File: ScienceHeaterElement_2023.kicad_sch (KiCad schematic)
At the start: 9 parts, among them Q1 NPN, U1 LMT85DCK

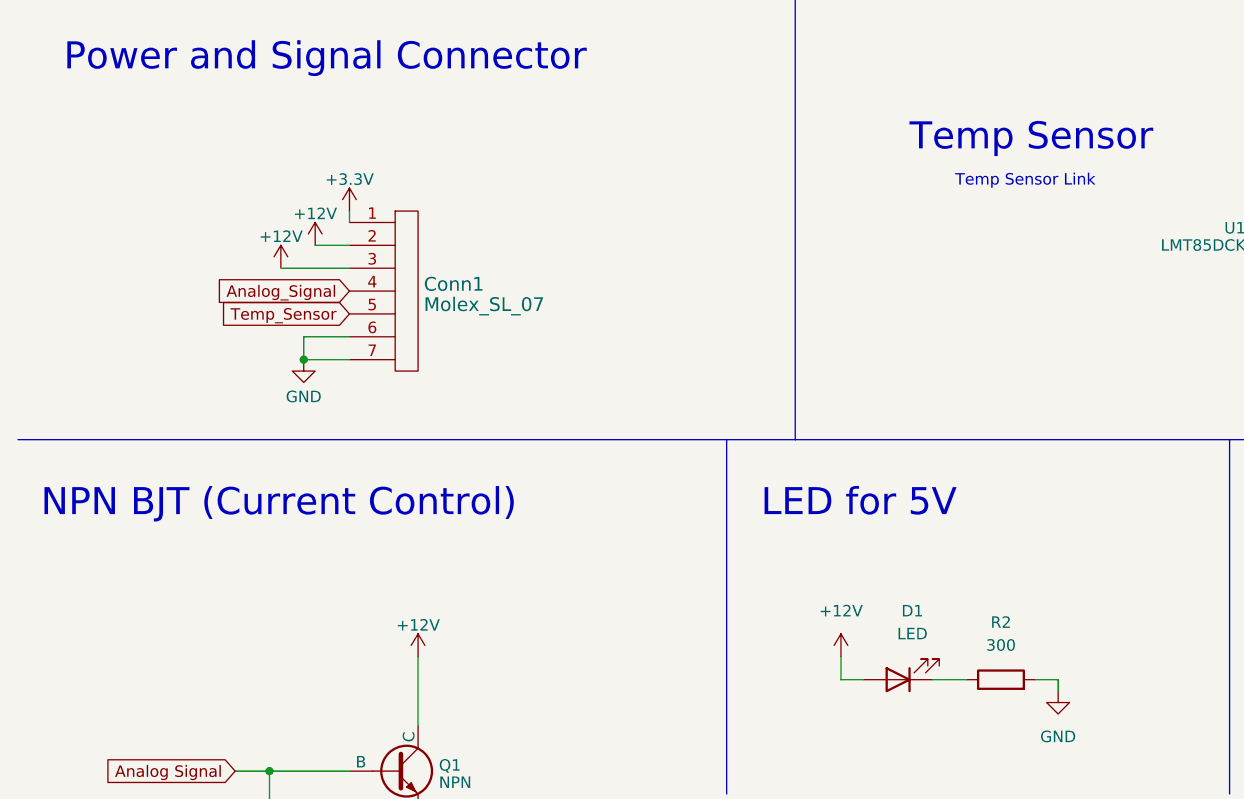
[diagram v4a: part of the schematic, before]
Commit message: Changed LED power and Molex 7 pin
Changed LED power from two 12V to a 12V and a 3.3V to indicate power of the two lines, and changed the molex 7 pin connector to a 3 pin and a 4 pin
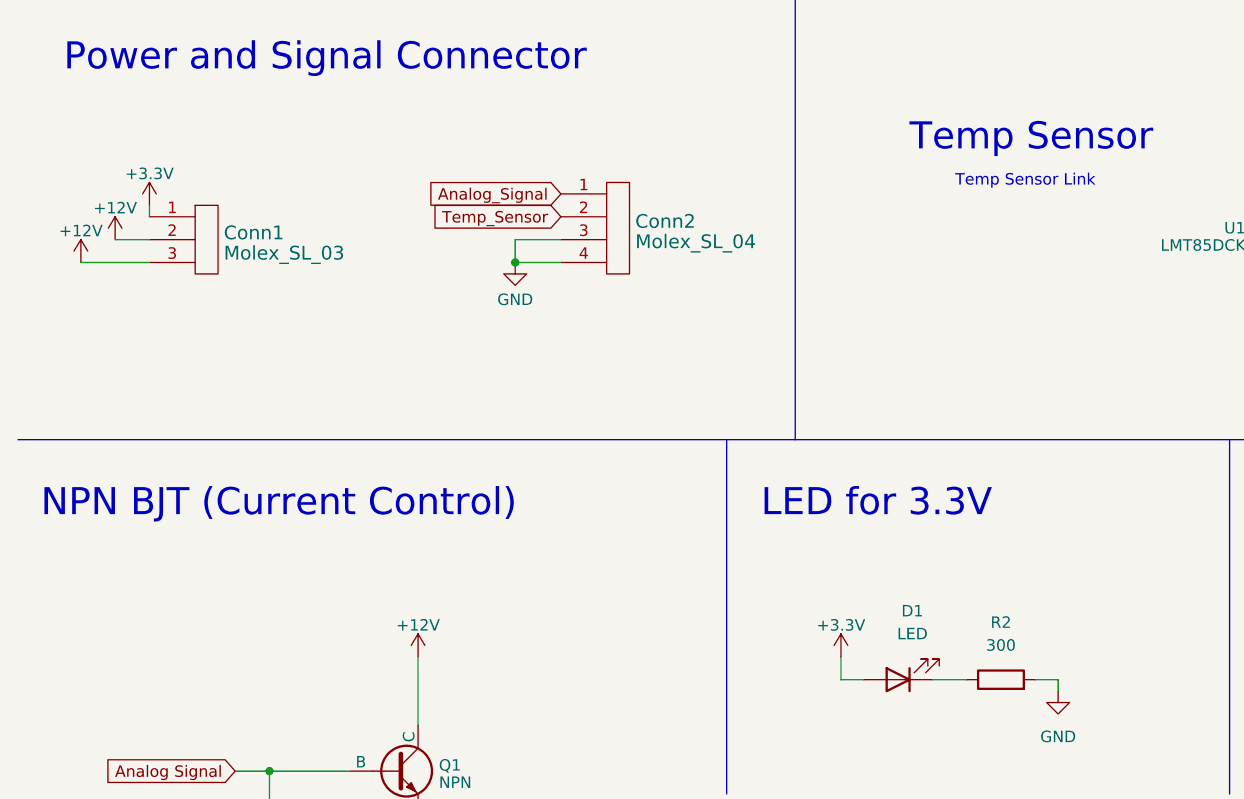
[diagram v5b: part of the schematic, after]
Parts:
- removed Conn1: Molex_SL_07, symbol MRDT_Connectors:Molex_SL_07
- added Conn1: Molex_SL_03, symbol MRDT_Connectors:Molex_SL_03
- added Conn2: Molex_SL_04, symbol MRDT_Connectors:Molex_SL_04
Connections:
- net +12V: now also Conn1.2, Conn1.3; no longer D1.2 (A)
- net +3.3V: now also D1.2 (A), Conn1.1
- net Analog_Signal: now also Conn2.1
- net GND: now also Conn2.3, Conn2.4
- net Temp_Sensor: now also Conn2.2
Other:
- note removed: "LED for 5V"

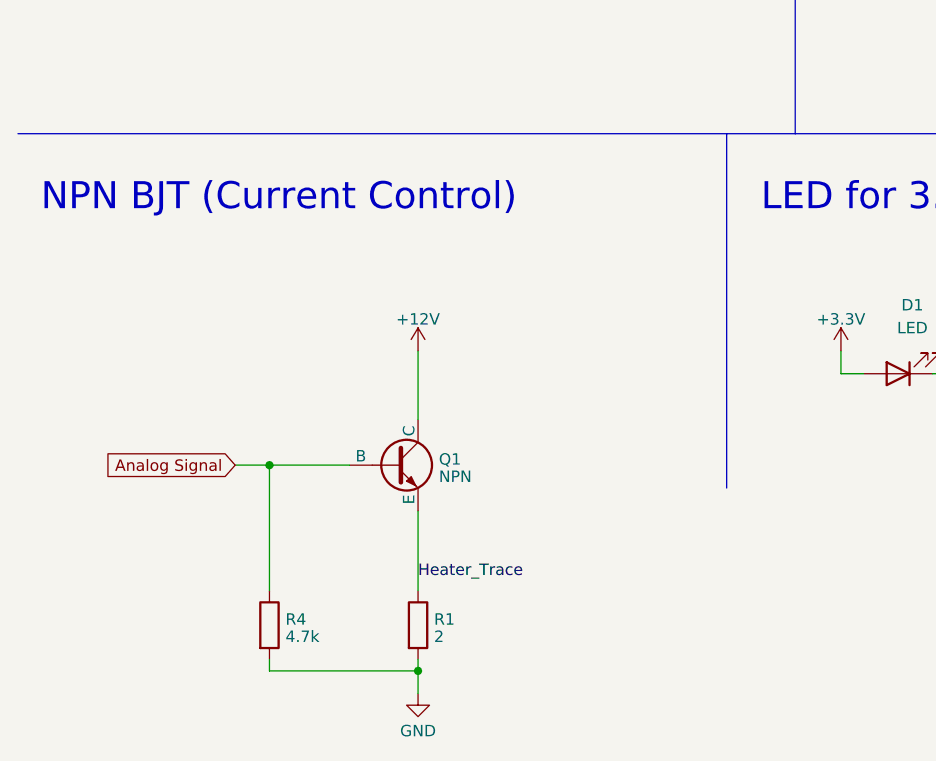
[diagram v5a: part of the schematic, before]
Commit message: Switched BJT to MOSFET
Switched to a MOSFET from a BJT. The testing for the BJT gave us unusable results for controlling the current flow through the BJT so we switched to a MOSFET which allows easier controls of the heating element
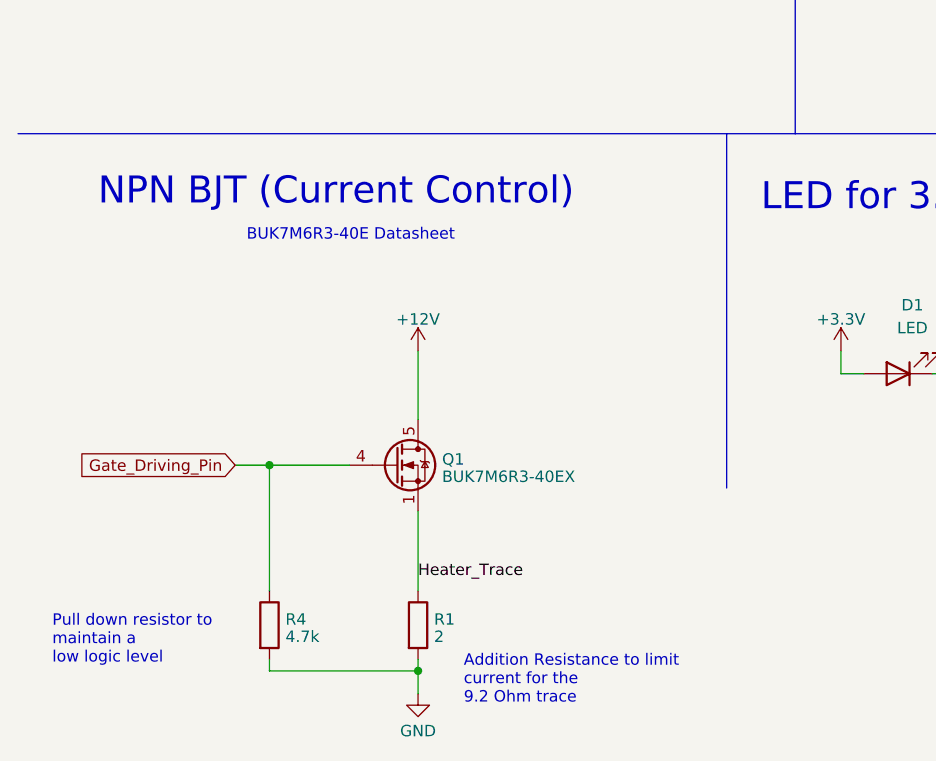
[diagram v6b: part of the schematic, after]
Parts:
- removed Q1: NPN, symbol Simulation_SPICE:NPN
- added Q1: BUK7M6R3-40EX, Package_TO_SOT_SMD:LFPAK33, symbol Transistor_FET:BUK7M6R3-40EX
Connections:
- net +12V: now also Q1.5 (D)
- net Heater_Trace: now also Q1.1 (S), Q1.2 (S), Q1.3 (S)
- net Analog Signal renamed Gate_Driving_Pin
- net Gate_Driving_Pin: now also Q1.4 (G)
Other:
- note added: "Addition Resistance to limit current for the 9.2 Ohm trace"
- note added: "BUK7M6R3-40E Datasheet"
- note added: "Pull down resistor to maintain a low logic level"
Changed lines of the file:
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@@
     (stroke (width 0) (type default))
+  )
+  (text "Addition Resistance to limit \ncurrent for the \n9.2 Ohm trace"
+    (at 60.96 128.27 0)
+    (effects (font (size 1.27 1.27)) (justify left bottom))
   )
   (text "LED for 3.3V" (at 149.86 72.39 0)
@@
     (effects (font (size 3 3)) (justify left bottom))
   )
-  (text "NPN BJT (Current Control)" (at 13.97 73.66 0)
+  (text "BUK7M6R3-40E Datasheet" (at 36.83 76.835 0)
+    (effects (font (size 1.27 1.27)) (justify left bottom) (href "https://assets.nexperia.com/documents/data-sheet/BUK7M6R3-40E.pdf"))
+  )
+  (text "NPN BJT (Current Control)" (at 20.32 73.025 0)
     (effects (font (size 3 3)) (justify left bottom))
   )
   (text "Temp Sensor" (at 110.49 33.02 0)
     (effects (font (size 3 3)) (justify left bottom))
+  )
+  (text "Pull down resistor to \nmaintain a \nlow logic level"
+    (at 15.24 123.825 0)
+    (effects (font (size 1.27 1.27)) (justify left bottom))
   )
   (label "Heater_Trace" (at 55.88 114.3 0) (fields_autoplaced)
@@
     )
   )
-  (global_label "Analog Signal" (shape input) (at 35.56 101.6 180) (fields_autoplaced)
+  (global_label "Gate_Driving_Pin" (shape input) (at 35.56 101.6 180) (fields_autoplaced)
     (effects (font (size 1.27 1.27)) (justify right))
-    (property "Intersheetrefs" "${INTERSHEET_REFS}" (at 19.4103 101.6 0)
+    (property "Intersheetrefs" "${INTERSHEET_REFS}" (at 16.9305 101.6 0)
       (effects (font (size 1.27 1.27)) (justify right) hide)
     )
@@
     )
   )
+  (symbol (lib_id "Transistor_FET:BUK7M6R3-40EX") (at 53.34 101.6 0) (unit 1)
+    (in_bom yes) (on_board yes) (dnp no) (fields_autoplaced)
+    (property "Reference" "Q1" (at 58.547 100.9563 0)
+      (effects (font (size 1.27 1.27)) (justify left))
+    )
+    (property "Value" "BUK7M6R3-40EX" (at 58.547 102.8773 0)
+      (effects (font (size 1.27 1.27)) (justify left))
+    )
+    (property "Footprint" "Package_TO_SOT_SMD:LFPAK33" (at 58.42 103.505 0)
+      (effects (font (size 1.27 1.27) italic) (justify left) hide)
+    )
+    (property "Datasheet" "https://assets.nexperia.com/documents/data-sheet/BUK7M6R3-40E.pdf" (at 53.34 101.6 90)
+      (effects (font (size 1.27 1.27)) (justify left) hide)
+    )
+    (pin "1")
+    (pin "2")
+    (pin "3")
+    (pin "4")
+    (pin "5")
+    (instances
+      (project "ScienceHeaterElement_2023"
+        (path "/e6c1e763-c694-4521-b530-f13b86f852cc"
+          (reference "Q1") (unit 1)
+        )
+      )
+    )
+  )
   (symbol (lib_id "power:+12V") (at 22.225 42.545 0) (unit 1)
     (in_bom yes) (on_board yes) (dnp no) (fields_autoplaced)
@@
         )
       )
-    )
-  )
-  (symbol (lib_id "Simulation_SPICE:NPN") (at 53.34 101.6 0) (unit 1)
-    (in_bom yes) (on_board yes) (dnp no) (fields_autoplaced)
-    (property "Reference" "Q1" (at 58.1914 100.9563 0)
-      (effects (font (size 1.27 1.27)) (justify left))
-    )
-    (property "Value" "NPN" (at 58.1914 102.8773 0)
-      (effects (font (size 1.27 1.27)) (justify left))
-    )
-    (property "Footprint" "" (at 116.84 101.6 0)
-      (effects (font (size 1.27 1.27)) hide)
-    )
-    (property "Datasheet" "~" (at 116.84 101.6 0)
-      (effects (font (size 1.27 1.27)) hide)
-    )
-    (property "Sim.Device" "NPN" (at 53.34 101.6 0)
-      (effects (font (size 1.27 1.27)) hide)
-    )
-    (property "Sim.Type" "GUMMELPOON" (at 53.34 101.6 0)
-      (effects (font (size 1.27 1.27)) hide)
-    )
-    (property "Sim.Pins" "1=C 2=B 3=E" (at 53.34 101.6 0)
-      (effects (font (size 1.27 1.27)) hide)
-    )
-    (pin "1")
-    (pin "2")
-    (pin "3")
-    (instances
-      (project "ScienceHeaterElement_2023"
-        (path "/e6c1e763-c694-4521-b530-f13b86f852cc"
-          (reference "Q1") (unit 1)
-        )
-      )

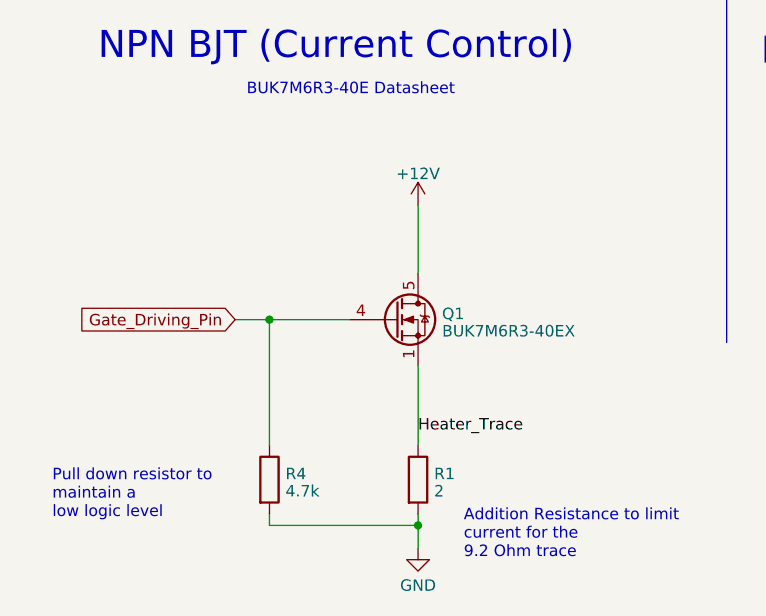
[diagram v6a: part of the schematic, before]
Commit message: Changed MOSFET Circuit to High Side toggle
Changed MOSFET Circuit to High Side toggling circuit to allow for proper control from the teensy
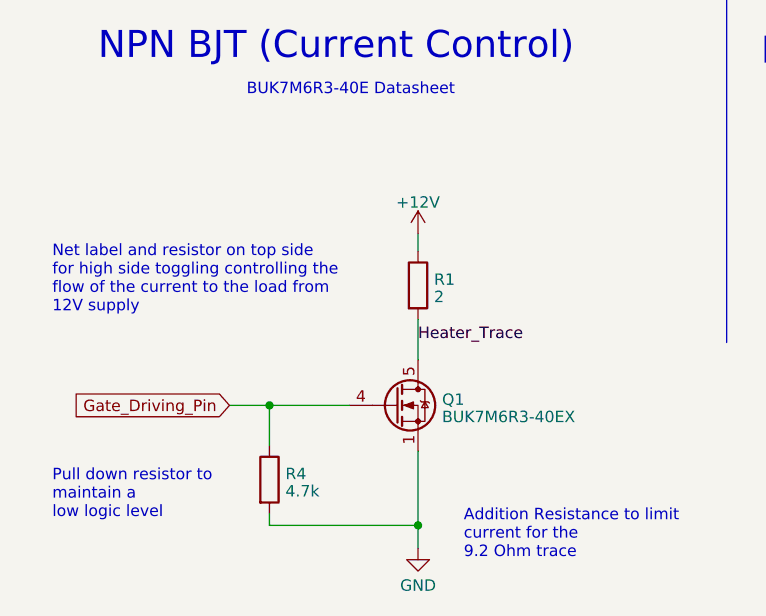
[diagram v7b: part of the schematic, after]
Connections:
- net +12V: now also R1.1; no longer Q1.5 (D)
- net GND: now also Q1.1 (S), Q1.2 (S), Q1.3 (S); no longer R1.2
- net Heater_Trace: now also Q1.5 (D), R1.2; no longer Q1.1 (S), Q1.2 (S), Q1.3 (S), R1.1
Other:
- note added: "Net label and resistor on top side for high side toggling controlling the flow of the current to the load from 12V supply"
- moved on the sheet: Q1
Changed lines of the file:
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@@
 (kicad_sch (version 20230121) (generator eeschema)
   (paper "A5")
+  (junction (at 39.37 111.125) (diameter 0) (color 0 0 0 0)
+  )
   (junction (at 154.94 34.29) (diameter 0) (color 0 0 0 0)
   )
   (junction (at 157.48 52.07) (diameter 0) (color 0 0 0 0)
   )
-  (junction (at 39.37 101.6) (diameter 0) (color 0 0 0 0)
-  )
   (junction (at 55.88 124.46) (diameter 0) (color 0 0 0 0)
   )
@@
     (stroke (width 0) (type default))
   )
-  (wire (pts (xy 39.37 101.6) (xy 48.26 101.6))
+  (wire (pts (xy 39.37 111.125) (xy 48.26 111.125))
     (stroke (width 0) (type default))
   )
@@
     (stroke (width 0) (type default))
   )
-  (wire (pts (xy 55.88 88.9) (xy 55.88 96.52))
-    (stroke (width 0) (type default))
-  )
-  (wire (pts (xy 35.56 101.6) (xy 39.37 101.6))
+  (wire (pts (xy 34.925 111.125) (xy 39.37 111.125))
     (stroke (width 0) (type default))
   )
@@
     (stroke (width 0) (type default))
   )
+  (wire (pts (xy 55.88 93.98) (xy 55.88 92.075))
+    (stroke (width 0) (type default))
+  )
   (wire (pts (xy 66.675 42.545) (xy 66.675 45.085))
     (stroke (width 0) (type default))
@@
     (stroke (width 0) (type default))
   )
+  (wire (pts (xy 55.88 101.6) (xy 55.88 106.045))
+    (stroke (width 0) (type default))
+  )
   (wire (pts (xy 127 91.44) (xy 127 92.71))
     (stroke (width 0) (type default))
@@
     (stroke (width 0) (type default))
   )
-  (wire (pts (xy 55.88 106.68) (xy 55.88 115.57))
-    (stroke (width 0) (type default))
-  )
   (wire (pts (xy 18.415 45.085) (xy 26.035 45.085))
     (stroke (width 0) (type default))
   )
-  (wire (pts (xy 55.88 123.19) (xy 55.88 124.46))
-    (stroke (width 0) (type default))
-  )
-  (wire (pts (xy 39.37 115.57) (xy 39.37 101.6))
+  (wire (pts (xy 39.37 115.57) (xy 39.37 111.125))
+    (stroke (width 0) (type default))
+  )
+  (wire (pts (xy 55.88 116.205) (xy 55.88 124.46))
     (stroke (width 0) (type default))
   )
@@
     (effects (font (size 3 3)) (justify left bottom))
   )
+  (text "Net label and resistor on top side\nfor high side toggling controlling the\nflow of the current to the load from \n12V supply"
+    (at 15.24 100.965 0)
+    (effects (font (size 1.27 1.27)) (justify left bottom))
+  )
   (text "Temp Sensor Link" (at 115.57 36.83 0)
     (effects (font (size 1.27 1.27)) (justify left bottom) (href "https://www.digikey.com/en/products/detail/texas-instruments/lmt85lp/4876348"))
@@
     (effects (font (size 1.27 1.27)) (justify left bottom))
   )
-  (label "Heater_Trace" (at 55.88 114.3 0) (fields_autoplaced)
+  (label "Heater_Trace" (at 55.88 104.14 0) (fields_autoplaced)
     (effects (font (size 1.27 1.27)) (justify left bottom))
   )
@@
     )
   )
-  (global_label "Gate_Driving_Pin" (shape input) (at 35.56 101.6 180) (fields_autoplaced)
+  (global_label "Gate_Driving_Pin" (shape input) (at 34.925 111.125 180) (fields_autoplaced)
     (effects (font (size 1.27 1.27)) (justify right))
-    (property "Intersheetrefs" "${INTERSHEET_REFS}" (at 16.9305 101.6 0)
+    (property "Intersheetrefs" "${INTERSHEET_REFS}" (at 16.2955 111.125 0)
       (effects (font (size 1.27 1.27)) (justify right) hide)
     )
@@
     )
   )
-  (symbol (lib_id "power:+12V") (at 55.88 88.9 0) (unit 1)
-    (in_bom yes) (on_board yes) (dnp no) (fields_autoplaced)
-    (property "Reference" "#PWR05" (at 55.88 92.71 0)
-      (effects (font (size 1.27 1.27)) hide)
-    )
-    (property "Value" "+12V" (at 55.88 85.3981 0)
-      (effects (font (size 1.27 1.27)))
-    )
-    (property "Footprint" "" (at 55.88 88.9 0)
-      (effects (font (size 1.27 1.27)) hide)
-    )
-    (property "Datasheet" "" (at 55.88 88.9 0)
+  (symbol (lib_id "power:+12V") (at 55.88 92.075 0) (unit 1)
+    (in_bom yes) (on_board yes) (dnp no) (fields_autoplaced)
+    (property "Reference" "#PWR05" (at 55.88 95.885 0)
+      (effects (font (size 1.27 1.27)) hide)
+    )
+    (property "Value" "+12V" (at 55.88 88.5731 0)
+      (effects (font (size 1.27 1.27)))
+    )
+    (property "Footprint" "" (at 55.88 92.075 0)
+      (effects (font (size 1.27 1.27)) hide)
+    )
+    (property "Datasheet" "" (at 55.88 92.075 0)
       (effects (font (size 1.27 1.27)) hide)
     )
@@
     )
   )
-  (symbol (lib_id "Transistor_FET:BUK7M6R3-40EX") (at 53.34 101.6 0) (unit 1)
-    (in_bom yes) (on_board yes) (dnp no) (fields_autoplaced)
-    (property "Reference" "Q1" (at 58.547 100.9563 0)
+  (symbol (lib_id "Transistor_FET:BUK7M6R3-40EX") (at 53.34 111.125 0) (unit 1)
+    (in_bom yes) (on_board yes) (dnp no) (fields_autoplaced)
+    (property "Reference" "Q1" (at 58.547 110.4813 0)
       (effects (font (size 1.27 1.27)) (justify left))
     )
-    (property "Value" "BUK7M6R3-40EX" (at 58.547 102.8773 0)
+    (property "Value" "BUK7M6R3-40EX" (at 58.547 112.4023 0)
       (effects (font (size 1.27 1.27)) (justify left))
     )
-    (property "Footprint" "Package_TO_SOT_SMD:LFPAK33" (at 58.42 103.505 0)
+    (property "Footprint" "Package_TO_SOT_SMD:LFPAK33" (at 58.42 113.03 0)
       (effects (font (size 1.27 1.27) italic) (justify left) hide)
     )
-    (property "Datasheet" "https://assets.nexperia.com/documents/data-sheet/BUK7M6R3-40E.pdf" (at 53.34 101.6 90)
+    (property "Datasheet" "https://assets.nexperia.com/documents/data-sheet/BUK7M6R3-40E.pdf" (at 53.34 111.125 90)
       (effects (font (size 1.27 1.27)) (justify left) hide)
     )
@@
     )
   )
-  (symbol (lib_id "Device:R") (at 55.88 119.38 0) (unit 1)
-    (in_bom yes) (on_board yes) (dnp no) (fields_autoplaced)
-    (property "Reference" "R1" (at 57.658 118.7363 0)
+  (symbol (lib_id "Device:R") (at 55.88 97.79 0) (unit 1)
+    (in_bom yes) (on_board yes) (dnp no) (fields_autoplaced)
+    (property "Reference" "R1" (at 57.658 97.1463 0)
       (effects (font (size 1.27 1.27)) (justify left))
     )
-    (property "Value" "2" (at 57.658 120.6573 0)
+    (property "Value" "2" (at 57.658 99.0673 0)
       (effects (font (size 1.27 1.27)) (justify left))
     )
-    (property "Footprint" "" (at 54.102 119.38 90)
-      (effects (font (size 1.27 1.27)) hide)
-    )
-    (property "Datasheet" "~" (at 55.88 119.38 0)
-      (effects (font (size 1.27 1.27)) hide)
-    )
+    (property "Footprint" "" (at 54.102 97.79 90)
+      (effects (font (size 1.27 1.27)) hide)
+    )
+    (property "Datasheet" "~" (at 55.88 97.79 0)
+      (effects (font (size 1.27 1.27)) hide)
+    )
